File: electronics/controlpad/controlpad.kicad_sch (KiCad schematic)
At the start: 23 parts, among them J1 USB - Host, SW10 0, SW11 8, SW12 10, SW13 11, SW14 12, SW15 13, SW16 14, SW17 15, SW2 1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

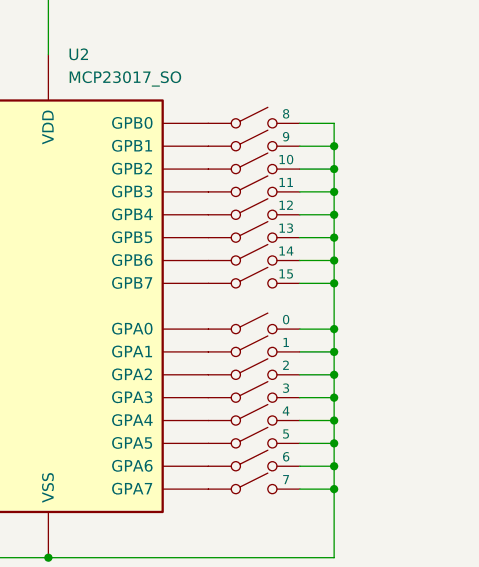
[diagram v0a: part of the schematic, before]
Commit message: Adding B15 as system/start button
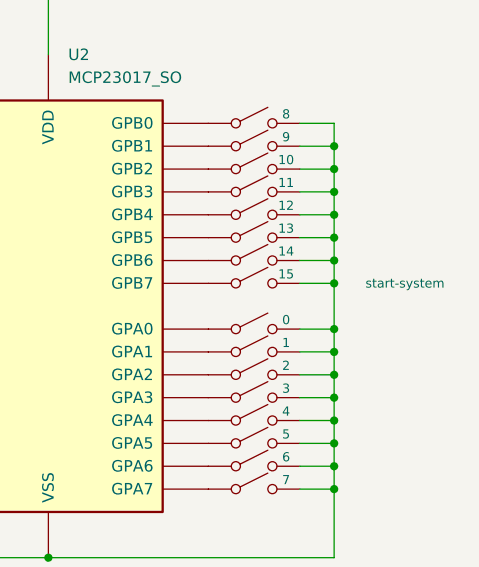
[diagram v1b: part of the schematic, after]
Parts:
- SW17: Field5 (none) -> start-system
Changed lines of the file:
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@@
+			"AAAAAAAAAAAAAAAAAAAAAAAAAAAAAAAAAAAAAAAAAAAAAAAAAAAAAAAAAAAAAAAAAAAAAAAAAAAA"
+			"AAAAAAAAAAAAAAAAAAAAAAAAAAAAAAAAAAAAAAAAAAAAAAAAAAAAAAAAAAAAAAAAAAAAAAAAAAAA"
+			"AAAAAAAAAAAAAAAAAAAAAAAAAAAAAAAAAAAAAAAAAAAAAAAAAAAAAAAAAAAAAAAAAAAAAAAAAAAA"
+			"AAAAAAAAAAAAAAAAAAAAAAAAAAAAAAAAAAAAAAAAAAAAAAAAAAAAAAAAAAAAAAAAAAAAAAAAAAAA"
+			"AAAAAAAAAAAAAAAAAAAAAAAAAAAAAAAAAAAAAAAAAAAAAAAAAAAAAAAAAAAAAAAAAAAAAAAAAAAA"
+			"AAAAAAAAAAAAAAAAAAAAAAAAAAAAAAAAAAAAAAAAAAAAAAAAAAAAAAAAAAAAAAAAAAAAAAAAAAAA"
+			"AAAAAAAAAAAAAAAAAAAAAAAAAAAAAAAAAAAAAAAAAAAAAAAAAAAAAAAAAAAAAAAAAAAAAAAAAAAA"
+			"AAAAAAAAAAAAAAAAAAAAAAAAAAAAAAAAAAAAAAAAAAAAAAAAAAAAAAAAAAAAAAAAAAAAAAAAAAAA"
+			"AAAAAAAAAAAAAAAAAAAAAAAAAAAAAAAAAAAAAAAAAAAAAAAAAAAAAAAAAAAAAAAAAAAAAAAAAAAA"
+			"AAAAAAAAAAAAAAAAAAAAAAAAAAAAAAAAAAAAAAAAAAAAAAAAAAAAAAAAAAAAAAAAAAAAAAAAAAAA"
+			"AAAAAAAAAAAAAAAAAAAAAAAAAAAAAAAAAAAAAAAAAAAAAAAAAAAAAAAAAAAAAAAAAAAAAAAAAAAA"
+			"AAAAAAAAAAAAAAAAAAAAAAAAAAAAAAAAAAAAAAAAAAAAAAAAAAAAAAAAAAAAAAAAAAAAAAAAAAAA"
+			"AAAAAAAAAAAAAAAAAAAAAAAAAAAAAAAAAAAAAAAAAAAAAAAAAAAAAAAAAAAAAAAAAAAAAAAAAAAA"
+			"AAAAAAAAAAAAAAAAAAAAAAAAAAAAAAAAAAAAAAAAAAAAAAAAAAAAAAAAAAAAAAAAAAAAAAAAAAAA"
+			"AAAAAAAAAAAAAAAAAAAAAAAAAAAAAAAAAAAAAAAAAAAAAAAAAAAAAAAAAAAAAAAAAAAAAAAAAAAA"
+			"AAAAAAAAAAAAAAAAAAAAAAAAAAAAAAAAAAAAAAAAAAAAAAAAAAAAAAAAAAAAAAAAAAAAAAAAAAAA"
+			"AAAAAAAAAAAAAAAAAAAAAAAAAAAAAAAAAAAAAAAAAAAAAAAAAAAAAAAAAAAAAAAAAAAAAAAAAAAA"
+			"AAAAAAAAAAAAAAAAAAAAAAAAAAAAAAAAAAAAAAAAAAAAAAAAAAAAAAAAAAAAAAAAAAAAAAAAAAAA"
 			"AAAAAAAAAAAAAAAAAAAAAAAAAAAAAAAAAAAAAAAAAAAAAAAAAAAAAAAAAAAAAAAAAAAAAAAAAAAA"
 			"AAAAAAAAAAAAAAAAAAAAAAAAAAAAAAAAAAAAAAAAAAAAAAAAAAAAAAAAAAAAAAAAAAAAAAAAAAAA"
@@
 			)
 		)
+		(property "Field5" "start-system"
+			(at 203.454 119.38 0)
+			(effects
+				(font
+					(size 1.016 1.016)
+				)
+			)
+		)
